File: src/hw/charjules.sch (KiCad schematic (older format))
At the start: 58 parts

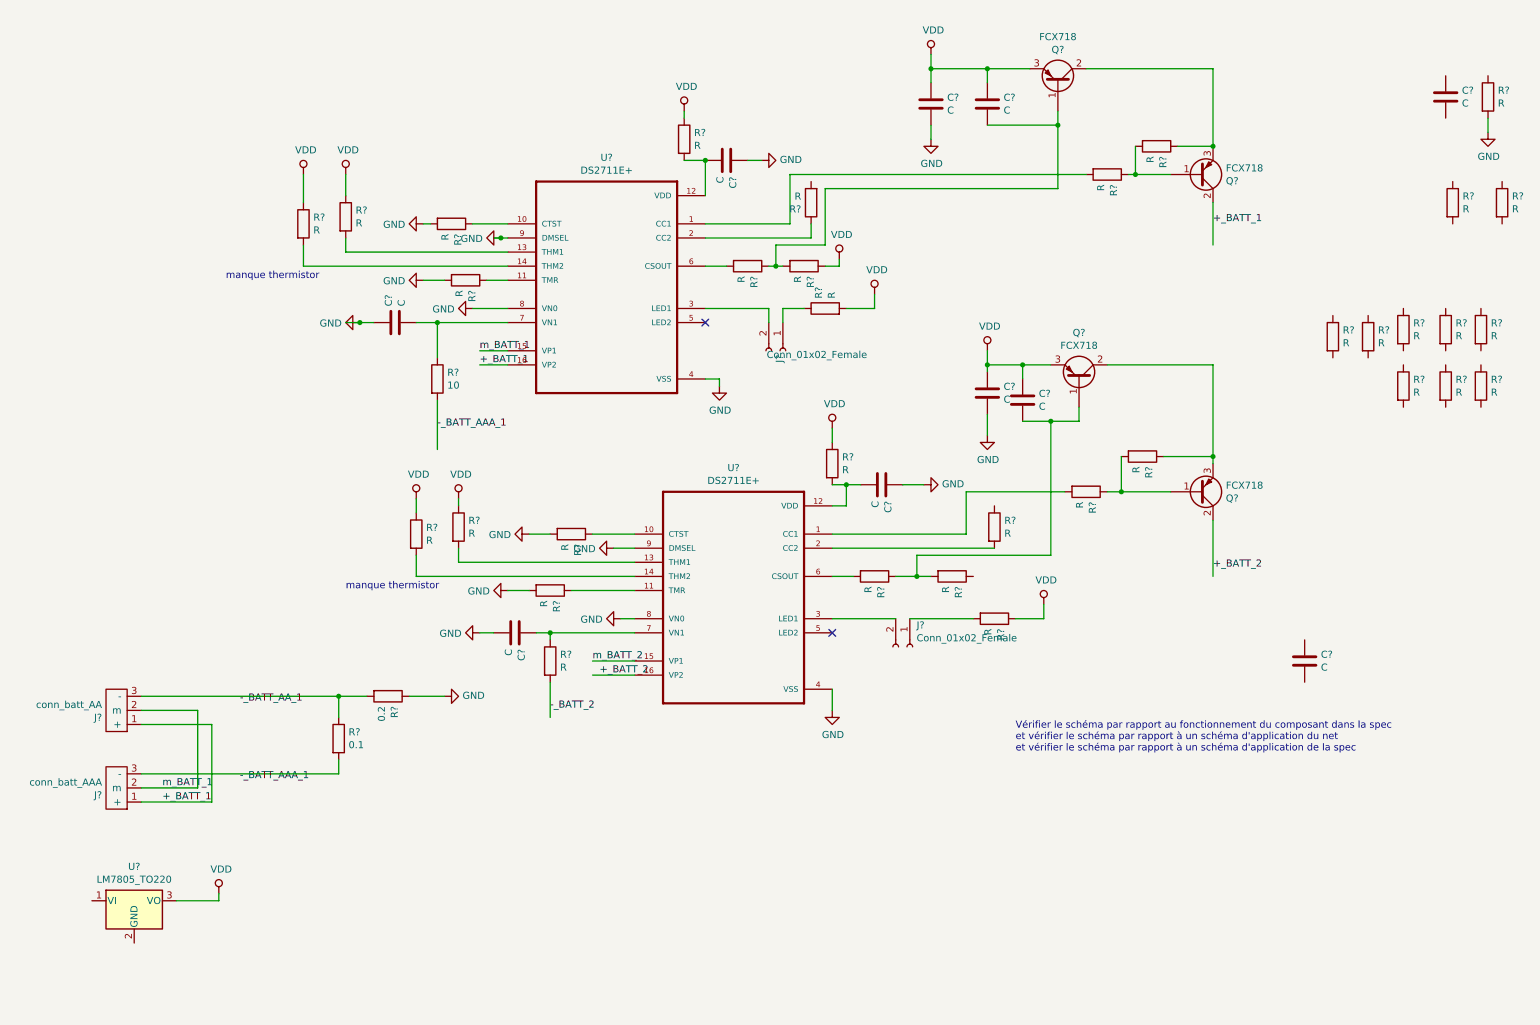
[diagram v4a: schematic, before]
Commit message: continue le schéma et doc #4 #6
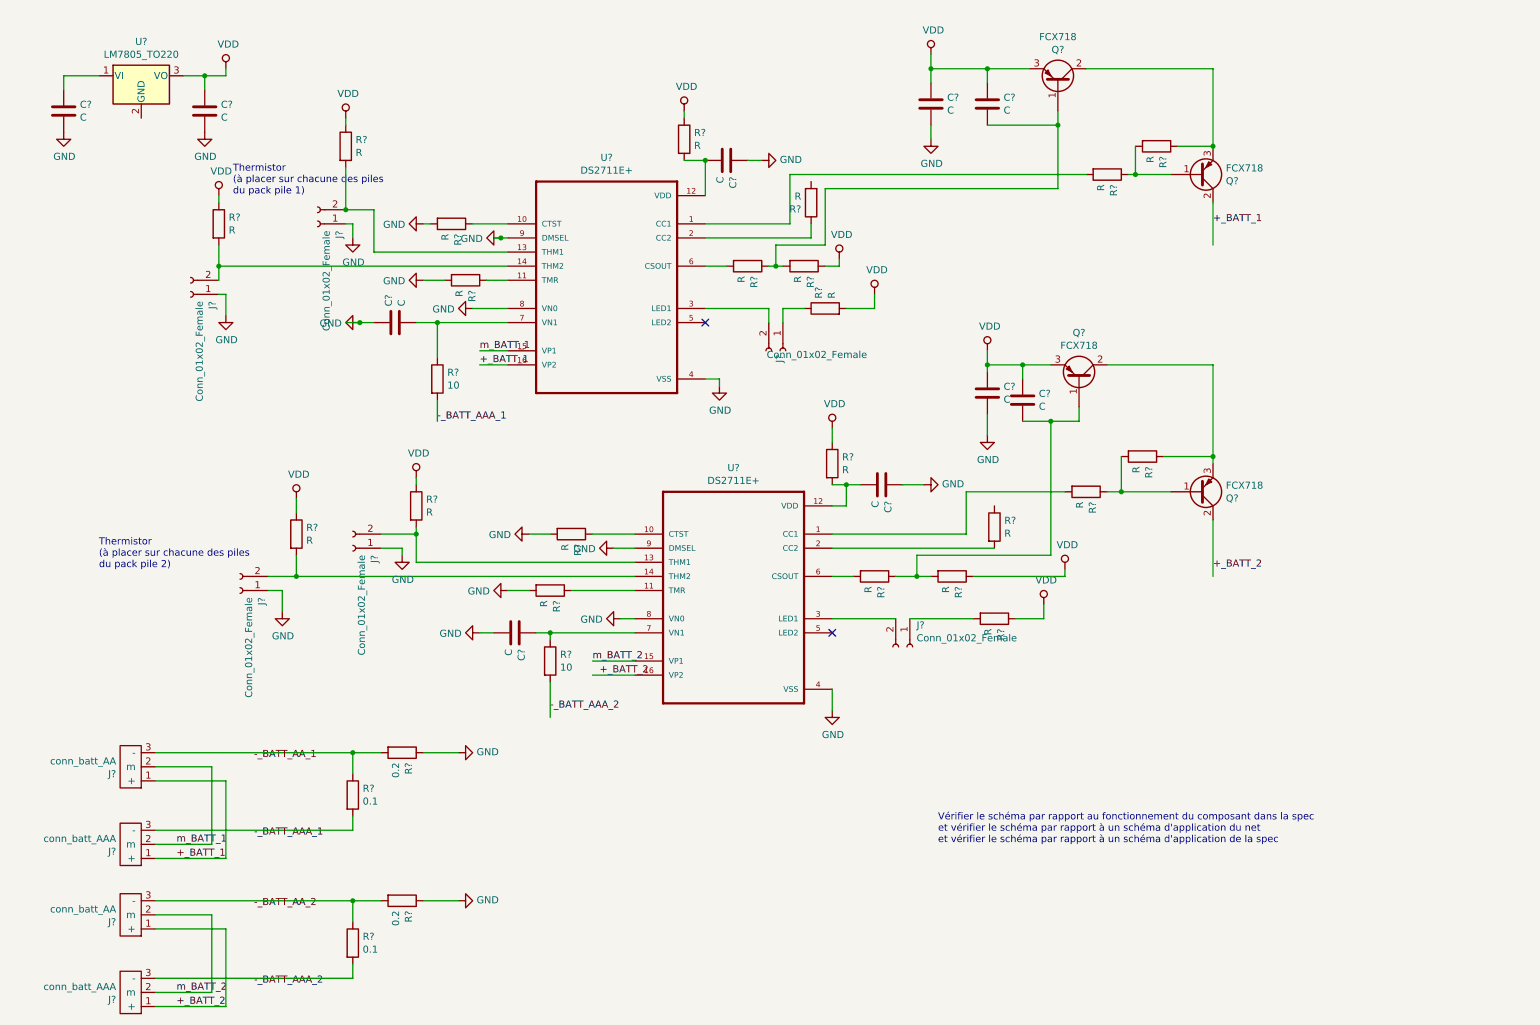
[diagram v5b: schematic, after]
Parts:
- removed R? (x11): R, symbol Device:R
- added J?: conn_batt_AA, symbol f4bjh:conn_batt_AA
- added J?: conn_batt_AAA, symbol f4bjh:conn_batt_AAA
- added J? (x4): Conn_01x02_Female, symbol Connector:Conn_01x02_Female
- added R?: 0.2, symbol Device:R
- added R?: 0.1, symbol Device:R
- R?: value R -> 10
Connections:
- net labels added: -_BATT_AAA_2, -_BATT_AA_2
- net labels removed: -_BATT_2
- wire segments 135 -> 166
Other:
- note added: "Thermistor \n(à placer sur chacune des piles\ndu pack pile 1)"
- note added: "Thermistor \n(à placer sur chacune des piles\ndu pack pile 2)"
- note removed: "manque thermistor"
- moved on the sheet: C?, J?, R?, U?

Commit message: continue le schéma #4 #5
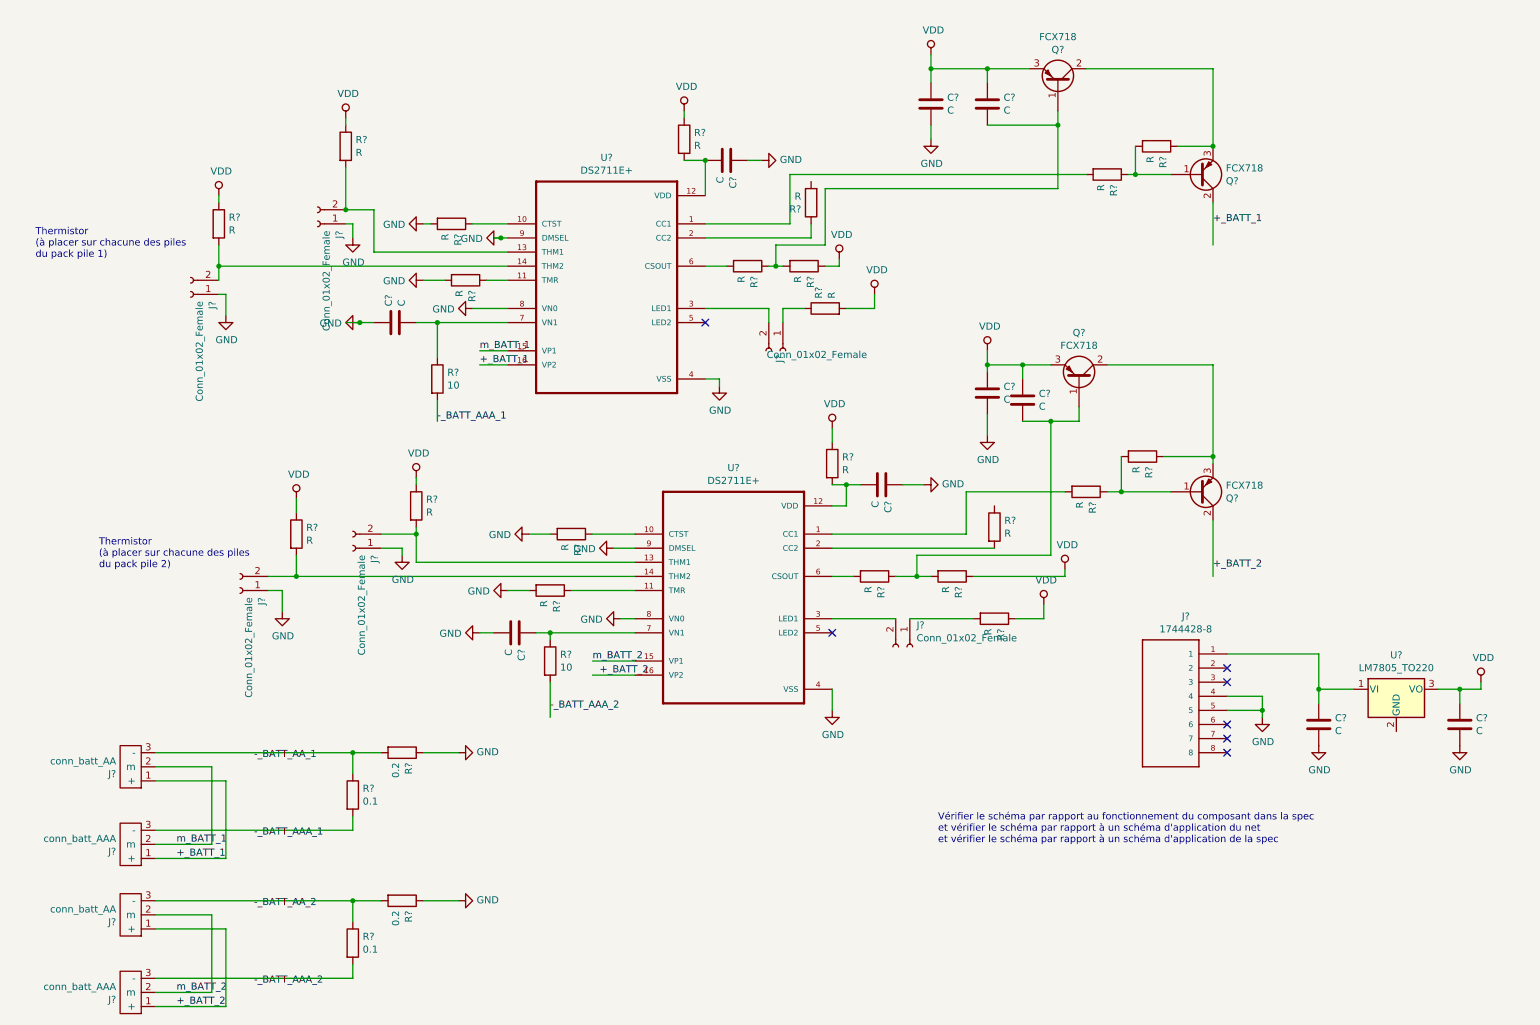
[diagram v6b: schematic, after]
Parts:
- added J?: 1744428-8, TE_1744428-8, symbol f4bjh:1744428-8
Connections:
- wire segments 166 -> 172
- no-connect marks 2 -> 7
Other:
- moved on the sheet: C?, U?
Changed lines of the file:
@@
 L Device:C C?
 U 1 1 5E180625
-P 1800 1250
-F 0 "C?" H 1915 1296 50  0000 L CNN
-F 1 "C" H 1915 1205 50  0000 L CNN
-F 2 "" H 1838 1100 50  0001 C CNN
-F 3 "~" H 1800 1250 50  0001 C CNN
-	1    1800 1250
+P 10700 5600
+F 0 "C?" H 10815 5646 50  0000 L CNN
+F 1 "C" H 10815 5555 50  0000 L CNN
+F 2 "" H 10738 5450 50  0001 C CNN
+F 3 "~" H 10700 5600 50  0001 C CNN
+	1    10700 5600
 	1    0    0    -1
 $EndComp
@@
 L Device:C C?
 U 1 1 5E185F23
-P 800 1250
-F 0 "C?" H 915 1296 50  0000 L CNN
-F 1 "C" H 915 1205 50  0000 L CNN
-F 2 "" H 838 1100 50  0001 C CNN
-F 3 "~" H 800 1250 50  0001 C CNN
-	1    800  1250
+P 9700 5600
+F 0 "C?" H 9815 5646 50  0000 L CNN
+F 1 "C" H 9815 5555 50  0000 L CNN
+F 2 "" H 9738 5450 50  0001 C CNN
+F 3 "~" H 9700 5600 50  0001 C CNN
+	1    9700 5600
 	1    0    0    -1
 $EndComp
@@
 L Regulator_Linear:LM7805_TO220 U?
 U 1 1 5E1FD6D9
-P 1350 1000
-F 0 "U?" H 1350 1242 50  0000 C CNN
-F 1 "LM7805_TO220" H 1350 1151 50  0000 C CNN
-F 2 "Package_TO_SOT_THT:TO-220-3_Vertical" H 1350 1225 50  0001 C CIN
-F 3 "http://www.fairchildsemi.com/ds/LM/LM7805.pdf" H 1350 950 50  0001 C CNN
-	1    1350 1000
+P 10250 5350
+F 0 "U?" H 10250 5592 50  0000 C CNN
+F 1 "LM7805_TO220" H 10250 5501 50  0000 C CNN
+F 2 "Package_TO_SOT_THT:TO-220-3_Vertical" H 10250 5575 50  0001 C CIN
+F 3 "http://www.fairchildsemi.com/ds/LM/LM7805.pdf" H 10250 5300 50  0001 C CNN
+	1    10250 5350
 	1    0    0    -1
 $EndComp
@@
 L power:VDD #PWR?
 U 1 1 5E20345A
-P 1950 950
-F 0 "#PWR?" H 1950 800 50  0001 C CNN
-F 1 "VDD" H 1967 1123 50  0000 C CNN
-F 2 "" H 1950 950 50  0001 C CNN
-F 3 "" H 1950 950 50  0001 C CNN
-	1    1950 950
-	1    0    0    -1
-$EndComp
-Wire Wire Line
-	1950 1000 1950 950
-Wire Wire Line
-	1650 1000 1800 1000
+P 10850 5300
+F 0 "#PWR?" H 10850 5150 50  0001 C CNN
+F 1 "VDD" H 10867 5473 50  0000 C CNN
+F 2 "" H 10850 5300 50  0001 C CNN
+F 3 "" H 10850 5300 50  0001 C CNN
+	1    10850 5300
+	1    0    0    -1
+$EndComp
+Wire Wire Line
+	10850 5350 10850 5300
+Wire Wire Line
+	10550 5350 10700 5350
 Wire Wire Line
 	5350 2050 5950 2050
@@
 L power:GND #PWR?
 U 1 1 5E464ECA
-P 1800 1400
-F 0 "#PWR?" H 1800 1150 50  0001 C CNN
-F 1 "GND" H 1805 1227 50  0000 C CNN
-F 2 "" H 1800 1400 50  0001 C CNN
-F 3 "" H 1800 1400 50  0001 C CNN
-	1    1800 1400
+P 10700 5750
+F 0 "#PWR?" H 10700 5500 50  0001 C CNN
+F 1 "GND" H 10705 5577 50  0000 C CNN
+F 2 "" H 10700 5750 50  0001 C CNN
+F 3 "" H 10700 5750 50  0001 C CNN
+	1    10700 5750
 	1    0    0    -1
 $EndComp
@@
 L power:GND #PWR?
 U 1 1 5E466A26
-P 800 1400
-F 0 "#PWR?" H 800 1150 50  0001 C CNN
-F 1 "GND" H 805 1227 50  0000 C CNN
-F 2 "" H 800 1400 50  0001 C CNN
-F 3 "" H 800 1400 50  0001 C CNN
-	1    800  1400
-	1    0    0    -1
-$EndComp
-Wire Wire Line
-	1800 1100 1800 1000
-Connection ~ 1800 1000
-Wire Wire Line
-	1800 1000 1950 1000
-Wire Wire Line
-	800  1100 800  1000
-Wire Wire Line
-	800  1000 1050 1000
+P 9700 5750
+F 0 "#PWR?" H 9700 5500 50  0001 C CNN
+F 1 "GND" H 9705 5577 50  0000 C CNN
+F 2 "" H 9700 5750 50  0001 C CNN
+F 3 "" H 9700 5750 50  0001 C CNN
+	1    9700 5750
+	1    0    0    -1
+$EndComp
+Wire Wire Line
+	10700 5450 10700 5350
+Connection ~ 10700 5350
+Wire Wire Line
+	10700 5350 10850 5350
+Wire Wire Line
+	9700 5450 9700 5350
+Wire Wire Line
+	9700 5350 9950 5350
 $Comp
 L Connector:Conn_01x02_Female J?
@@
 Wire Wire Line
 	2800 1650 2800 1950
-Text Notes 2000 1850 0    50   ~ 0
+Text Notes 600  2300 0    50   ~ 0
 Thermistor \n(à placer sur chacune des piles\ndu pack pile 1)
 Wire Wire Line
@@
 Text Notes 1050 4500 0    50   ~ 0
 Thermistor \n(à placer sur chacune des piles\ndu pack pile 2)
+$Comp
+L f4bjh:1744428-8 J?
+U 1 1 5E7A084F
+P 8650 5500
+F 0 "J?" H 8543 6167 50  0000 C CNN
+F 1 "1744428-8" H 8543 6076 50  0000 C CNN
+F 2 "TE_1744428-8" H 8650 5500 50  0001 L BNN
+F 3 "Compliant" H 8650 5500 50  0001 L BNN
+F 4 "https://www.te.com/usa-en/product-1744428-8.html?te_bu=Cor&te_type=disp&te_campaign=seda_glo_cor-seda-global-disp-prtnr-fy19-seda-model-bom-cta_sma-317_1&elqCampaignId=32493" H 8650 5500 50  0001 L BNN "Champ4"
+F 5 "1744428-8" H 8650 5500 50  0001 L BNN "Champ5"
+	1    8650 5500
+	-1   0    0    -1
+$EndComp
+$Comp
+L power:GND #PWR?
+U 1 1 5E7AA6D1
+P 9300 5550
+F 0 "#PWR?" H 9300 5300 50  0001 C CNN
+F 1 "GND" H 9305 5377 50  0000 C CNN
+F 2 "" H 9300 5550 50  0001 C CNN
+F 3 "" H 9300 5550 50  0001 C CNN
+	1    9300 5550
+	1    0    0    -1
+$EndComp
+Wire Wire Line
+	9050 5500 9300 5500
+Wire Wire Line
+	9300 5500 9300 5550
+Wire Wire Line
+	9050 5400 9300 5400
+Wire Wire Line
+	9300 5400 9300 5500
+Connection ~ 9300 5500
+Wire Wire Line
+	9050 5100 9700 5100
+Wire Wire Line
+	9700 5100 9700 5350
+Connection ~ 9700 5350
+NoConn ~ 9050 5200
+NoConn ~ 9050 5300
+NoConn ~ 9050 5600
+NoConn ~ 9050 5700
+NoConn ~ 9050 5800
 $EndSCHEMATC

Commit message: oubli GND sur régulateur #4
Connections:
- wire segments 172 -> 173
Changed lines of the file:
@@
 NoConn ~ 9050 5700
 NoConn ~ 9050 5800
+$Comp
+L power:GND #PWR?
+U 1 1 5E805C54
+P 10250 5750
+F 0 "#PWR?" H 10250 5500 50  0001 C CNN
+F 1 "GND" H 10255 5577 50  0000 C CNN
+F 2 "" H 10250 5750 50  0001 C CNN
+F 3 "" H 10250 5750 50  0001 C CNN
+	1    10250 5750
+	1    0    0    -1
+$EndComp
+Wire Wire Line
+	10250 5650 10250 5750
 $EndSCHEMATC

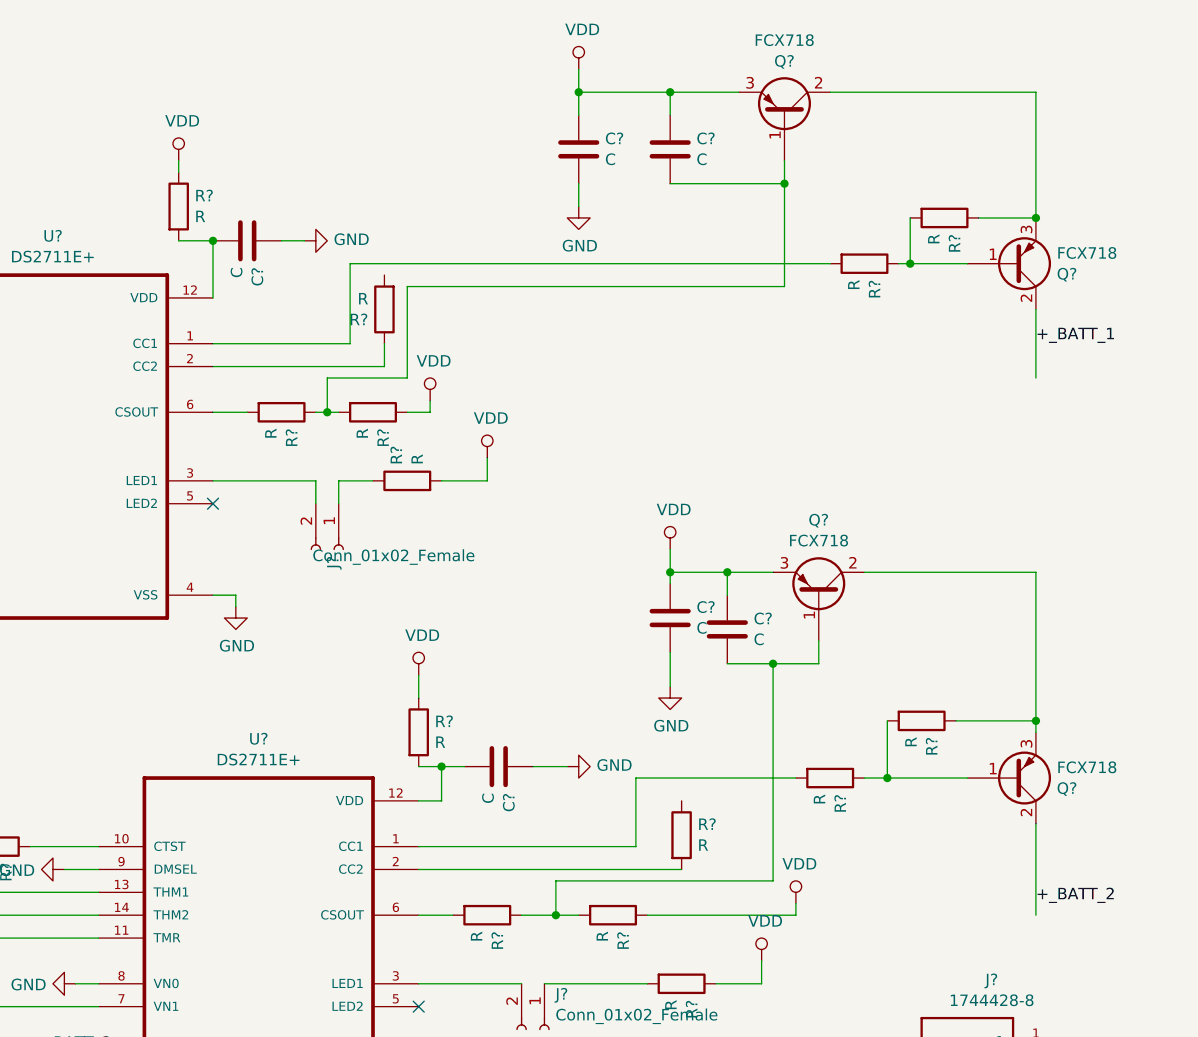
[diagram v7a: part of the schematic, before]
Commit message: continue le schéma : commence à remplir les valeurs des composants. Corrige les erreurs vis à vis de la spec #2 #4
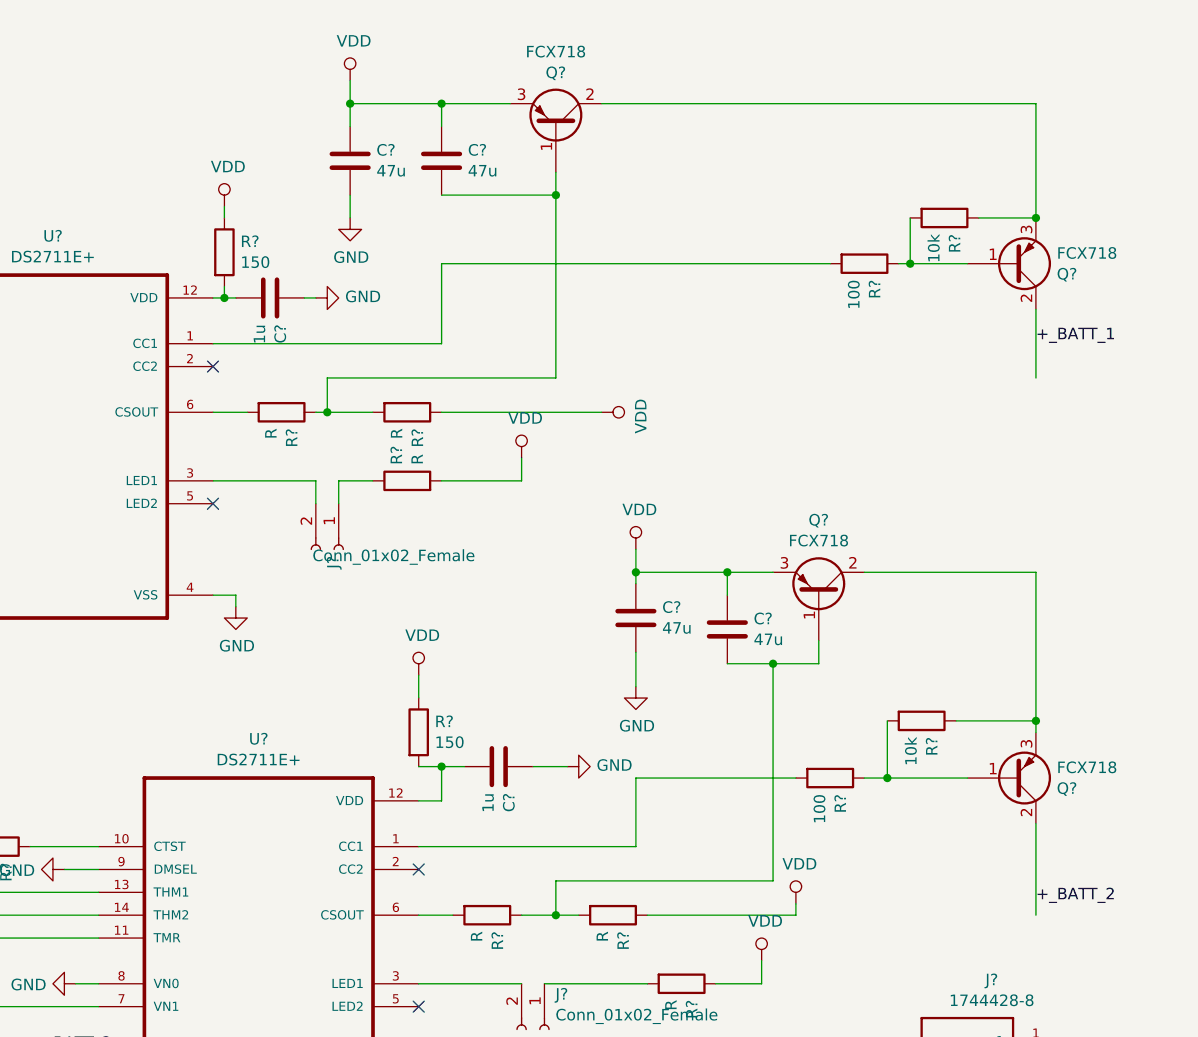
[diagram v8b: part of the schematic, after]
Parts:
- removed R? (x2): R, symbol Device:R
- C? (x4): value C -> 47u
- C? (x2): value C -> 1u
- R? (x2): value R -> 150
- R? (x2): value R -> 10k
- R? (x2): value R -> 100
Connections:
- wire segments 173 -> 168
- no-connect marks 7 -> 9
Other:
- moved on the sheet: C?, Q?, R?
